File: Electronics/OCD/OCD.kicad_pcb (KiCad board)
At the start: 2 copper layers, 100 x 86 mm, 61 parts, among them J1 TE-CK-6.35-29B, J2 Barrel_Jack_Switch, J3 PJ-645C MONO, SW1 SW_3PDT_x3, U1 TL074H, U2 TL074H

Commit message: RevA release
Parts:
- added C13: 220uF, Capacitor_SMD:CP_Elec_8x10, B.Cu at (80.0, 88.2)
- moved R17 140.7 mm to (92.4, 119.5)
- moved C12 140.7 mm to (78.8, 122.8)
- moved U1 140.6 mm to (85.8, 122.8)
- moved R25 118.8 mm to (70.4, 109.8), turned to 0 degrees
- moved R4 97.6 mm to (85.6, 130.5)
- moved R2 90.6 mm to (92.6, 130.5), turned to 0 degrees
- moved R3 90.6 mm to (92.6, 126.8)
- moved C3 87.3 mm to (85.5, 138.0)
- moved R5 85.2 mm to (85.6, 134.2)
- moved D3 83.5 mm to (97.2, 107.5)
- moved D2 80.8 mm to (102.2, 107.5)
- moved R11 80.0 mm to (120.2, 75.2)
- moved C11 80.0 mm to (120.2, 78.8)
- moved R12 79.6 mm to (120.2, 90.0)
- moved R26 79.3 mm to (134.5, 82.5)
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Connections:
- D4 pad 1: Net-(D4-K) -> Net-(D2-A)
- D4 pad 2: Net-(D2-A) -> Net-(D4-A)
- D5 pad 1: Net-(D4-K) -> Net-(D4-A)
- RV4 pad 3B: Net-(D4-K) -> Net-(D4-A)
- SW1 pad 7: unconnected-(SW1C-A-Pad7) -> /input_raw
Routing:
- net JGND: track 0.00 -> 290.8 mm, vias 0 -> 62
- net VGND: track 0.00 -> 195.0 mm, vias 0 -> 4
- net +9V: track 0.00 -> 174.1 mm, vias 0 -> 6
- net /Clipper Circuit/Output: track 0.00 -> 152.6 mm, vias 0 -> 2
- net /Clipper Circuit/bias: track 0.00 -> 116.0 mm, vias 0 -> 1
- net Net-(U1C--): track 0.00 -> 106.4 mm, vias 0 -> 2
- net Net-(R13-Pad2): track 0.00 -> 96.1 mm
- net Net-(D2-A): track 0.00 -> 93.0 mm, vias 0 -> 1
- net Net-(U1C-+): track 0.00 -> 85.9 mm, vias 0 -> 2
- net Net-(BT1-+): track 0.00 -> 78.3 mm, vias 0 -> 1
- net /Clipper Circuit/clipped: track 0.00 -> 76.5 mm, vias 0 -> 1
- net /input_buf: track 0.00 -> 75.2 mm, vias 0 -> 2
- net Net-(U1D--): track 0.00 -> 64.0 mm
- net Net-(SW1B-C): track 0.00 -> 57.3 mm, vias 0 -> 1
- net Net-(R12-Pad2): track 0.00 -> 55.4 mm, vias 0 -> 1
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- added copper zone on B.Cu, net JGND
- added copper zone on F.Cu, net JGND
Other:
- board text added: "${COMPANY} ${TITLE} Rev${REVISION} ${CURRENT_DATE}"
- board text added: "(LED)"
- board text added: "+"
- board text added: "-"
- board text added: "1"
- board text added: "2"
- board text added: "3"
- board text added: "4"
- board text added: "5"
- board text added: "6"
- board text added: "7"
- board text added: "8"
- board text added: "9"
- board text added: "9V BAT"
- board text added: "BATT (RING)"
- board text added: "CENTER-POSITIVE"
- board text added: "DC JACK"
- board text added: "GND (SLEEVE)"
- board text added: "GND (TS)"
- board text added: "INPUT"
- board text added: "LED"
- board text added: "OUTPUT"
- board text added: "SIG (TIP)"
- board text added: "SLEEVE (+9V)"
- board text added: "SWITCH (BAT+)"
- board text added: "TIP (GND)"
- board text added: "X"

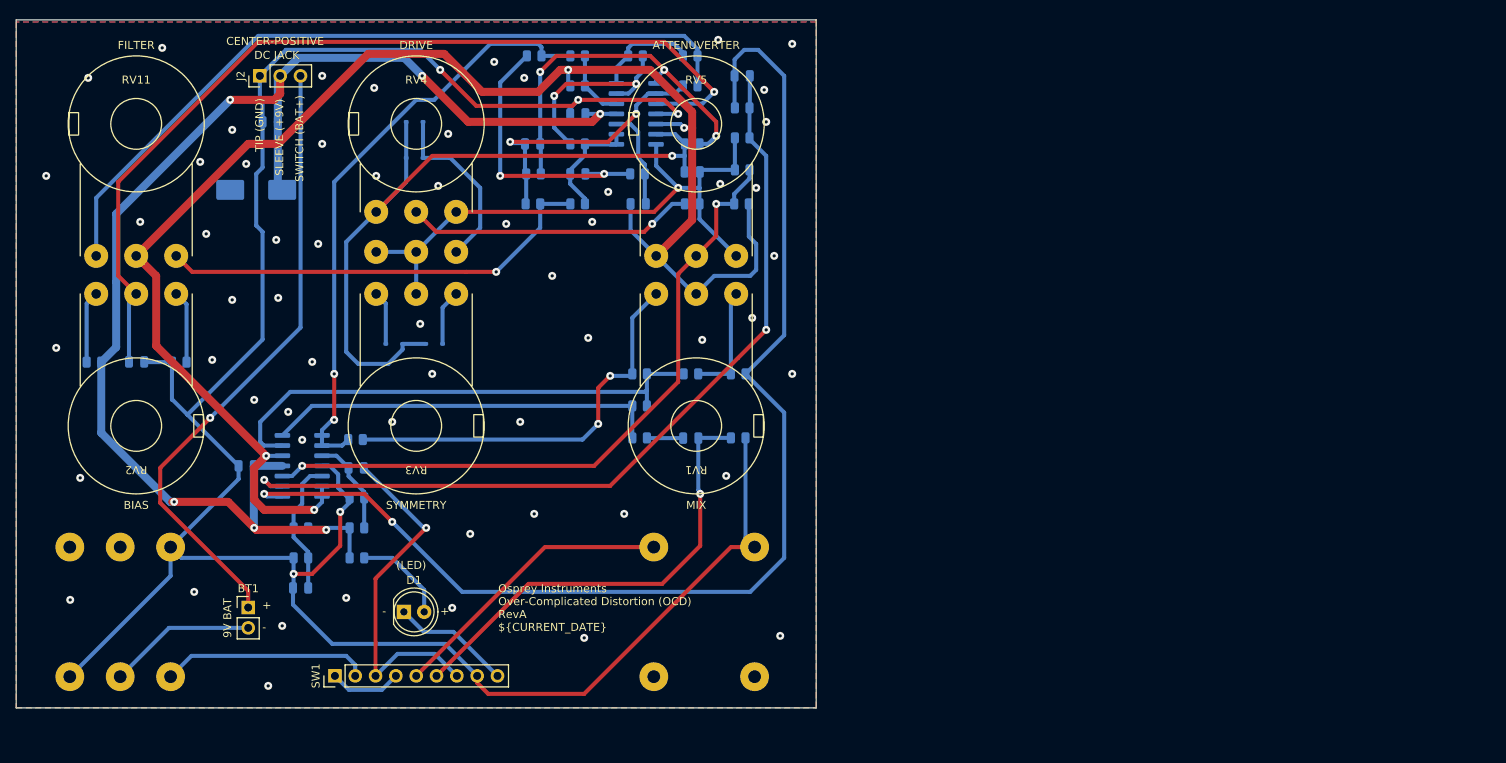
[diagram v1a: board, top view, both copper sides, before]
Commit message: RevB release. Corrected opamp orientation, added pad switch
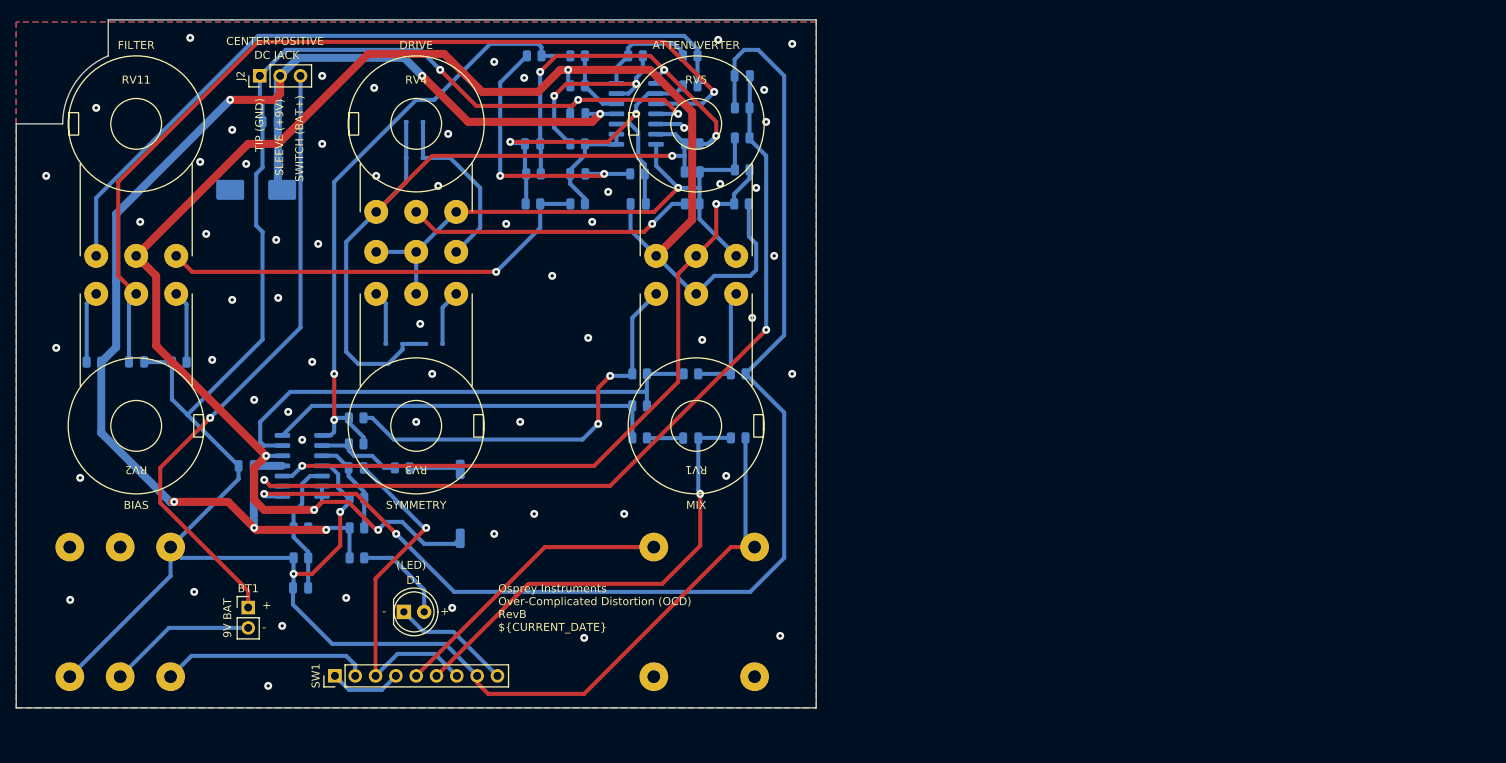
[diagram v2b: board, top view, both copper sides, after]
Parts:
- added R32: 100k, Resistor_SMD:R_0805_2012Metric, B.Cu at (92.5, 120.0)
- added R33: 10k, Resistor_SMD:R_0805_2012Metric, B.Cu at (98.2, 123.0)
- added SW2: SW_DIP_x01, Button_Switch_SMD:SW_DIP_SPSTx01_Slide_6.7x4.1mm_W8.61mm_P2.54mm_LowProfile, B.Cu at (105.5, 127.5)
- C7: value 1nF -> 47pF
- C8: value 220pF -> 47pF
- R19: value 47K -> 10k
- R20: value 100k -> 10k
- R23, R24, R25: value 100k -> 150k
- moved R17 2.71 mm to (92.5, 116.8)
- turned U1 to 0 degrees
- turned U2 to 0 degrees
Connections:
- C2 pad 2: Net-(U1A-+) -> Net-(U1C-+)
- C3 pad 1: Net-(U1B-+) -> Net-(U1D-+)
- C4 pad 2: Net-(U2C-+) -> Net-(U2A-+)
- C7 pad 2: Net-(U2A--) -> Net-(U2C--)
- C9 pad 2: Net-(U1C--) -> Net-(U1A--)
- R10 pad 1: Net-(U2D--) -> Net-(U2B--)
- R11 pad 2: Net-(U2D-+) -> Net-(U2B-+)
- R14 pad 2: Net-(U2A--) -> Net-(U2C--)
- R15 pad 2: Net-(U2A--) -> Net-(U2C--)
- R18 pad 2: Net-(U1D--) -> Net-(U1B--)
- R19 pad 2: Net-(U1D--) -> Net-(U1B--)
- R2 pad 2: Net-(U1A-+) -> Net-(U1C-+)
- R20 pad 1: Net-(U1D--) -> Net-(U1B--)
- R23 pad 1: Net-(U2A--) -> Net-(U2C--)
- R28 pad 1: Net-(U1C-+) -> Net-(U1A-+)
- R29 pad 2: Net-(U1C-+) -> Net-(U1A-+)
- R3 pad 1: Net-(U1A-+) -> Net-(U1C-+)
- R30 pad 1: Net-(U1C--) -> Net-(U1A--)
- R31 pad 2: Net-(U1C--) -> Net-(U1A--)
- R4 pad 2: Net-(U1B-+) -> Net-(U1D-+)
- R5 pad 1: Net-(U1B-+) -> Net-(U1D-+)
- R7 pad 2: Net-(U2C-+) -> Net-(U2A-+)
- R8 pad 2: Net-(U2D--) -> Net-(U2B--)
- R9 pad 2: Net-(U2D-+) -> Net-(U2B-+)
- RV5 pad 2: Net-(U1C-+) -> Net-(U1A-+)
- U1 pad 1: /input_buf -> /Clipper Circuit/Output
- U1 pad 11: +9V -> JGND
- U1 pad 12: VGND -> Net-(U1D-+)
- U1 pad 13: Net-(U1D--) -> VGND
- U1 pad 14: Net-(R20-Pad2) -> VGND
- U1 pad 2: /input_buf -> Net-(U1A--)
- U1 pad 4: JGND -> +9V
- U1 pad 5: Net-(U1B-+) -> VGND
- U1 pad 6: VGND -> Net-(U1B--)
- U1 pad 7: VGND -> Net-(R20-Pad2)
- U1 pad 8: /Clipper Circuit/Output -> /input_buf
- U2 pad 1: /Clipper Circuit/filtered -> /Clipper Circuit/LPF
- U2 pad 10: Net-(U2C-+) -> /Clipper Circuit/bias
- U2 pad 11: +9V -> JGND
- U2 pad 12: Net-(U2D-+) -> VGND
- U2 pad 13: Net-(U2D--) -> Net-(D2-A)
- U2 pad 14: /Clipper Circuit/HPF -> /Clipper Circuit/clipped
- U2 pad 2: Net-(U2A--) -> /Clipper Circuit/LPF
- U2 pad 3: /Clipper Circuit/bias -> Net-(U2A-+)
- U2 pad 4: JGND -> +9V
- U2 pad 5: VGND -> Net-(U2B-+)
- U2 pad 6: Net-(D2-A) -> Net-(U2B--)
- U2 pad 7: /Clipper Circuit/clipped -> /Clipper Circuit/HPF
- U2 pad 8: /Clipper Circuit/LPF -> /Clipper Circuit/filtered
- U2 pad 9: /Clipper Circuit/LPF -> Net-(U2C--)
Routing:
- net Net-(U1A--): track 0.00 -> 106.4 mm, vias 0 -> 2
- net Net-(U1C--): track 106.4 -> 10.9 mm, vias 2 -> 0
- net Net-(U1C-+): track 85.9 -> 12.3 mm, vias 2 -> 0
- net Net-(U1A-+): track 12.3 -> 85.9 mm, vias 0 -> 2
- net Net-(U1D--): track 64.0 -> 0.00 mm
- net Net-(U1B--): track 0.00 -> 64.0 mm
- net Net-(U2C--): track 0.00 -> 34.6 mm, vias 0 -> 2
- net Net-(U2A--): track 34.6 -> 0.00 mm, vias 2 -> 0
- net Net-(U2D--): track 24.7 -> 0.00 mm, vias 2 -> 0
- net Net-(U2B--): track 0.00 -> 24.7 mm, vias 0 -> 2
- net VGND: track 195.0 -> 217.0 mm, vias 4 -> 5
- net Net-(U1D-+): track 0.00 -> 17.1 mm
- net Net-(U1B-+): track 17.1 -> 0.00 mm
- net Net-(U2C-+): track 12.5 -> 0.00 mm
- net Net-(U2A-+): track 0.00 -> 12.5 mm
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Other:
- outline, holes or cut-outs redrawn
- board text added: "HIGH-Z"
- board text added: "LINE"
- board text added: "PAD"
